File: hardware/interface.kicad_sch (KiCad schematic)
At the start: 23 parts, among them P1 TS2068_Edge, SW1 TS Reset, SW2 NMI, U1 74LVC245APW, U2 74LVC245APW, U3 74LVC245APW, U4 74LVC245APW, U5 74LVC04APW, U6 74LVC08APW, U7 74LVC06APW, U8 74LVC126APW, U9 74LVC1G86

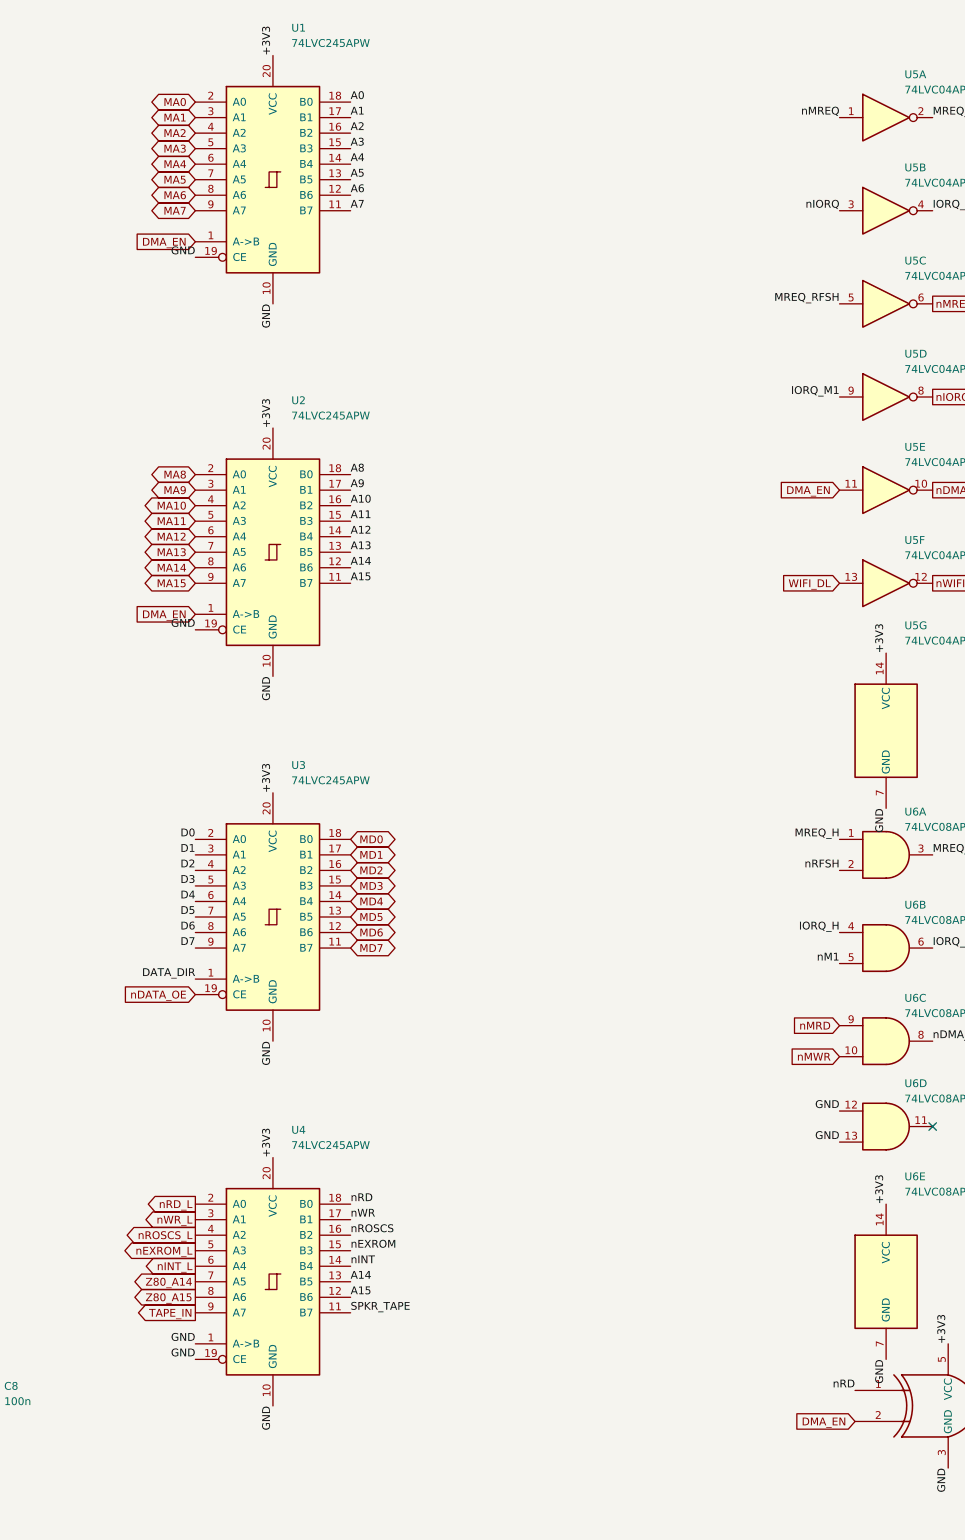
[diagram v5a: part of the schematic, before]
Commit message: Layout: transceivers in finger order with matching bit assignments, RP2350B rotated, MD block compacted
- gen_interface.py: 74LVC245 bit assignments follow the connector's pin order;
  U3 Z80 side moved to B, DATA_DIR = nRD xor nDMA_EN
- gen_layout.py: data/address/control transceivers under their fingers,
  muxes+registers in one row, U20 rotated 90 (MD corner toward the rows),
  keepout allows vias

Co-Authored-By: Claude Fable 5.1 <noreply@anthropic.com>
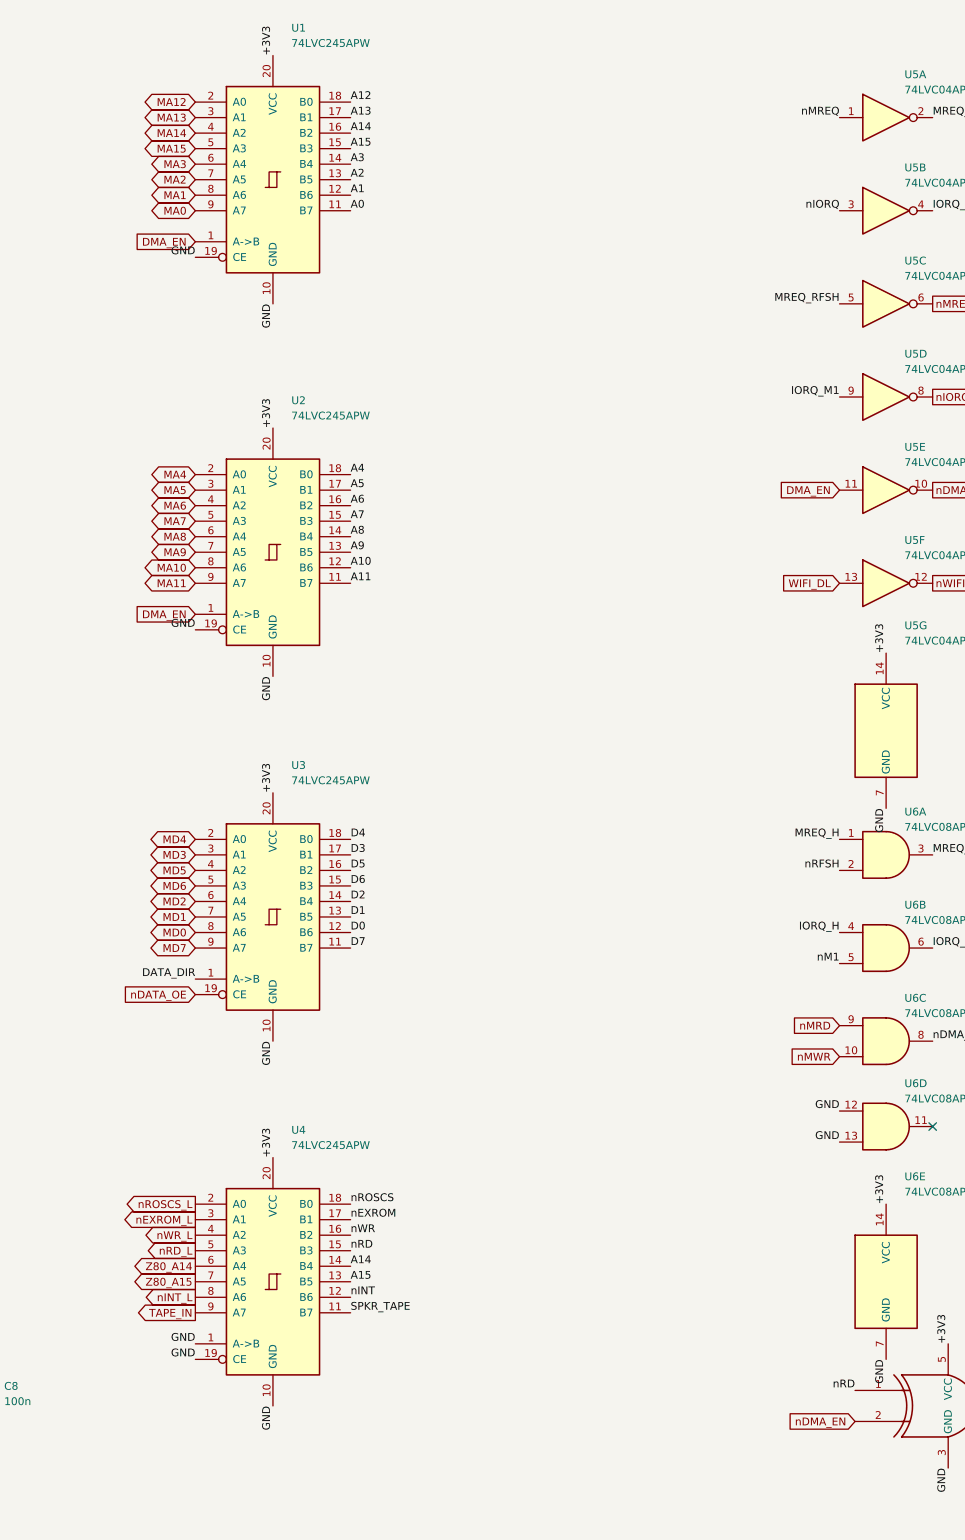
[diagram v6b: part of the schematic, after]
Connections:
- net A0: now also U1.11 (B7); no longer U1.18 (B0)
- net A1: now also U1.12 (B6); no longer U1.17 (B1)
- net A10: now also U2.12 (B6); no longer U2.16 (B2)
- net A11: now also U2.11 (B7); no longer U2.15 (B3)
- net A12: now also U1.18 (B0); no longer U2.14 (B4)
- net A13: now also U1.17 (B1); no longer U2.13 (B5)
- net A14: now also U1.16 (B2), U4.14 (B4); no longer U2.12 (B6), U4.13 (B5)
- net A15: now also U1.15 (B3), U4.13 (B5); no longer U2.11 (B7), U4.12 (B6)
- net A2: now also U1.13 (B5); no longer U1.16 (B2)
- net A3: now also U1.14 (B4); no longer U1.15 (B3)
- net A4: now also U2.18 (B0); no longer U1.14 (B4)
- net A5: now also U2.17 (B1); no longer U1.13 (B5)
- net A6: now also U2.16 (B2); no longer U1.12 (B6)
- net A7: now also U2.15 (B3); no longer U1.11 (B7)
- net A8: now also U2.14 (B4); no longer U2.18 (B0)
- net A9: now also U2.13 (B5); no longer U2.17 (B1)
- net D0: now also U3.12 (B6); no longer U3.2 (A0)
- net D1: now also U3.13 (B5); no longer U3.3 (A1)
- net D2: now also U3.14 (B4); no longer U3.4 (A2)
- net D3: now also U3.17 (B1); no longer U3.5 (A3)
- net D4: now also U3.18 (B0); no longer U3.6 (A4)
- net D5: now also U3.16 (B2); no longer U3.7 (A5)
- net D6: now also U3.15 (B3); no longer U3.8 (A6)
- net D7: now also U3.11 (B7); no longer U3.9 (A7)
- net DMA_EN: no longer U9.2
- net MA0: now also U1.9 (A7); no longer U1.2 (A0)
- net MA1: now also U1.8 (A6); no longer U1.3 (A1)
- net MA10: now also U2.8 (A6); no longer U2.4 (A2)
- net MA11: now also U2.9 (A7); no longer U2.5 (A3)
- net MA12: now also U1.2 (A0); no longer U2.6 (A4)
- net MA13: now also U1.3 (A1); no longer U2.7 (A5)
- net MA14: now also U1.4 (A2); no longer U2.8 (A6)
- net MA15: now also U1.5 (A3); no longer U2.9 (A7)
- net MA2: now also U1.7 (A5); no longer U1.4 (A2)
- net MA3: now also U1.6 (A4); no longer U1.5 (A3)
- net MA4: now also U2.2 (A0); no longer U1.6 (A4)
- net MA5: now also U2.3 (A1); no longer U1.7 (A5)
- net MA6: now also U2.4 (A2); no longer U1.8 (A6)
- net MA7: now also U2.5 (A3); no longer U1.9 (A7)
- net MA8: now also U2.6 (A4); no longer U2.2 (A0)
- net MA9: now also U2.7 (A5); no longer U2.3 (A1)
- net MD0: now also U3.8 (A6); no longer U3.18 (B0)
- net MD1: now also U3.7 (A5); no longer U3.17 (B1)
- net MD2: now also U3.6 (A4); no longer U3.16 (B2)
- net MD3: now also U3.3 (A1); no longer U3.15 (B3)
- net MD4: now also U3.2 (A0); no longer U3.14 (B4)
- net MD5: now also U3.4 (A2); no longer U3.13 (B5)
- net MD6: now also U3.5 (A3); no longer U3.12 (B6)
- net MD7: now also U3.9 (A7); no longer U3.11 (B7)
- net Z80_A14: now also U4.6 (A4); no longer U4.7 (A5)
- net Z80_A15: now also U4.7 (A5); no longer U4.8 (A6)
- net nDMA_EN: now also U9.2
- net nEXROM: now also U4.17 (B1); no longer U4.15 (B3)
- net nEXROM_L: now also U4.3 (A1); no longer U4.5 (A3)
- net nINT: now also U4.12 (B6); no longer U4.14 (B4)
- net nINT_L: now also U4.8 (A6); no longer U4.6 (A4)
- net nRD: now also U4.15 (B3); no longer U4.18 (B0)
- net nRD_L: now also U4.5 (A3); no longer U4.2 (A0)
- net nROSCS: now also U4.18 (B0); no longer U4.16 (B2)
- net nROSCS_L: now also U4.2 (A0); no longer U4.4 (A2)
- net nWR: now also U4.16 (B2); no longer U4.17 (B1)
- net nWR_L: now also U4.4 (A2); no longer U4.3 (A1)

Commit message: BOM cost optimisation against the JLCPCB catalog; schematic-side regulator fix
jlc_price.py prices the BOM via JLCPCB's parts API. Substitutions cut parts+fees
per board from $32.95 to $17.19 on a 10-board run: PSRAM DNP, electrolytic bulk
caps, TF-01A socket, PJ-320D jack, 74HC574, GD25Q128E, 0603 10 uF, basic LED,
preferred MCP6002; U16 decoder deleted (strobes on GPIO), U8 and U15 become
74LVC245s; J3/J5 hand-soldered. Adds the AOTA inductor and VREG_AVDD filter.
PCB needs a relayout; fab/ is stale.

Co-Authored-By: Claude Fable 5.1 <noreply@anthropic.com>
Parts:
- removed U8: 74LVC126APW, Package_SO:TSSOP-14_4.4x5mm_P0.65mm, symbol 74xx:74LS126
- added U8: 74LVC245APW, Package_SO:TSSOP-20_4.4x6.5mm_P0.65mm, symbol 74xx:74LS245
- U5: LCSC C7806 -> C54561939; MPN SN74LVC04APWRG4 -> SN74LVC04APWR-TP
- U6: LCSC C465737 -> C6053; MPN SN74LVC08APWR -> 74LVC08APW,118
- U7: value 74LVC06APW -> 74LVC06AD; footprint Package_SO:TSSOP-14_4.4x5mm_P0.65mm -> Package_SO:SOIC-14_3.9x8.7mm_P1.27mm; LCSC C131311 -> C49188178; MPN 74LVC06APW,118 -> EM74LVC06AD
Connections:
- net +3V3: now also U8.1 (A->B), U8.20 (VCC)
- net GND: now also U8.10 (GND), U8.5 (A3), U8.6 (A4), U8.7 (A5), U8.8 (A6), U8.9 (A7)
- net nDMA_EN: now also U8.19 (CE)
- net nDMA_MREQ: now also U8.2 (A0)
- net nMRD: now also U8.3 (A1)
- net nMREQ: now also U8.18 (B0)
- net nMWR: now also U8.4 (A2)
- net nRD: now also U8.17 (B1)
- net nWR: now also U8.16 (B2)
- no-connect marks 16 -> 20

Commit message: Logic consolidation: 15 packages to 8 fitted
Address buffers' output enables replace the 74LVC257 byte muxes and the MA bus;
one 74LVC32 makes MEMRD/MEMWR/IORD/IOWR strobes (replaces the 04 and 08);
XL9555 I2C expander replaces the CTL register, its power-on clear and the STAT
buffer; DMA parts are a DNP stuffing option (config.DMA_OPTION), with 74LVC574
latches directly on the address bus. GPIO map, architecture doc and cost notes
updated. Parts + fees per board now $14.93 on a 10-board run.

Co-Authored-By: Claude Fable 5.1 <noreply@anthropic.com>
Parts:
- removed U5: 74LVC04APW, Package_SO:TSSOP-14_4.4x5mm_P0.65mm, symbol 74xx:74LS04
- removed U6: 74LVC08APW, Package_SO:TSSOP-14_4.4x5mm_P0.65mm, symbol 74xx:74LS08
- added C9: 100n, Capacitor_SMD:C_0603_1608Metric, symbol Device:C
- added R4: 10k, Resistor_SMD:R_0603_1608Metric, symbol Device:R
- added U12, U13: 74LVC574APW, Package_SO:TSSOP-20_4.4x6.5mm_P0.65mm, symbol 74xx:74LS574
- added U6: 74LVC32APW, Package_SO:TSSOP-14_4.4x5mm_P0.65mm, symbol 74xx:74LS32
- C7, C8, U8: now not fitted
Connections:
- net DMA_EN is gone; now on net GND: U1.1 (A->B), U2.1 (A->B)
- net MA0 is gone; now on net MD0: U1.9 (A7)
- net MA1 is gone; now on net MD1: U1.8 (A6)
- net MA10 is gone; now on net MD6: U2.8 (A6)
- net MA11 is gone; now on net MD7: U2.9 (A7)
- net MA12 is gone; now on net MD4: U1.2 (A0)
- net MA13 is gone; now on net MD5: U1.3 (A1)
- net MA14 is gone; now on net MD6: U1.4 (A2)
- net MA15 is gone; now on net MD7: U1.5 (A3)
- net MA2 is gone; now on net MD2: U1.7 (A5)
- net MA3 is gone; now on net MD3: U1.6 (A4)
- net MA4 is gone; now on net MD0: U2.2 (A0)
- net MA5 is gone; now on net MD1: U2.3 (A1)
- net MA6 is gone; now on net MD2: U2.4 (A2)
- net MA7 is gone; now on net MD3: U2.5 (A3)
- net MA8 is gone; now on net MD4: U2.6 (A4)
- net MA9 is gone; now on net MD5: U2.7 (A5)
- net +3V3: now also C9.1, R4.1, U12.20 (VCC), U13.20 (VCC), U6.14 (VCC)
- net A0: now also U12.19 (Q0)
- net A1: now also U12.18 (Q1)
- net A10: now also U13.17 (Q2)
- net A11: now also U13.16 (Q3)
- net A12: now also U13.15 (Q4)
- net A13: now also U13.14 (Q5)
- net A14: now also U13.13 (Q6)
- net A15: now also U13.12 (Q7)
- net A2: now also U12.17 (Q2)
- net A3: now also U12.16 (Q3)
- net A4: now also U12.15 (Q4)
- net A5: now also U12.14 (Q5)
- net A6: now also U12.13 (Q6)
- net A7: now also U12.12 (Q7)
- net A8: now also U13.19 (Q0)
- net A9: now also U13.18 (Q1)
- net GND: now also U4.16 (B2), C9.2, U12.10 (GND), U13.10 (GND), U6.7 (GND); no longer U1.19 (CE), U2.19 (CE), U7.13
- net MD0: now also U12.2 (D0), U13.2 (D0)
- net MD1: now also U12.3 (D1), U13.3 (D1)
- net MD2: now also U12.4 (D2), U13.4 (D2)
- net MD3: now also U12.5 (D3), U13.5 (D3)
- net MD4: now also U12.6 (D4), U13.6 (D4)
- net MD5: now also U12.7 (D5), U13.7 (D5)
- net MD6: now also U12.8 (D6), U13.8 (D6)
- net MD7: now also U12.9 (D7), U13.9 (D7)
- net WIFI_DL: now also U7.13
- net nBUSAK: now also U4.15 (B3)
- net nDMA_EN: now also R4.2, U12.1 (OE), U13.1 (OE)
- net nIORQ: now also U6.12, U6.9
- net nMREQ: now also U6.1, U6.4
- net nRD: now also U6.10, U6.2; no longer U4.15 (B3)
- net nWIFI_BOOT: now also U7.12
- net nWR: now also U6.13, U6.5; no longer U4.16 (B2)
- net nM1: no longer names the net of P1.A25 (~{M1})
- net nRD_L renamed nBUSAK_L
- net nRFSH: no longer names the net of P1.A26 (~{RFSH})
- net nWR_L: no longer names the net of U4.4 (A2)
- new net nAEN_X: U1.19 (CE)
- new net nAEN_Y: U2.19 (CE)
- new net nIORD: U6.8
- new net nIOWR: U6.11
- new net nMEMRD: U6.3
- new net nMEMWR: U6.6
- new net nWR_AHI: U13.11 (Cp)
- new net nWR_ALO: U12.11 (Cp)
- no-connect marks 20 -> 21
